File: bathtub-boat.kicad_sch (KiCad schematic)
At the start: 22 parts, among them J1 I2C, J2 SPI, J3 I2C, J4 DS18B20, SW1 MODE, SW2 RESET, SW3 POWER, SW4 A, U1 esp-01m, U2 tp4056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

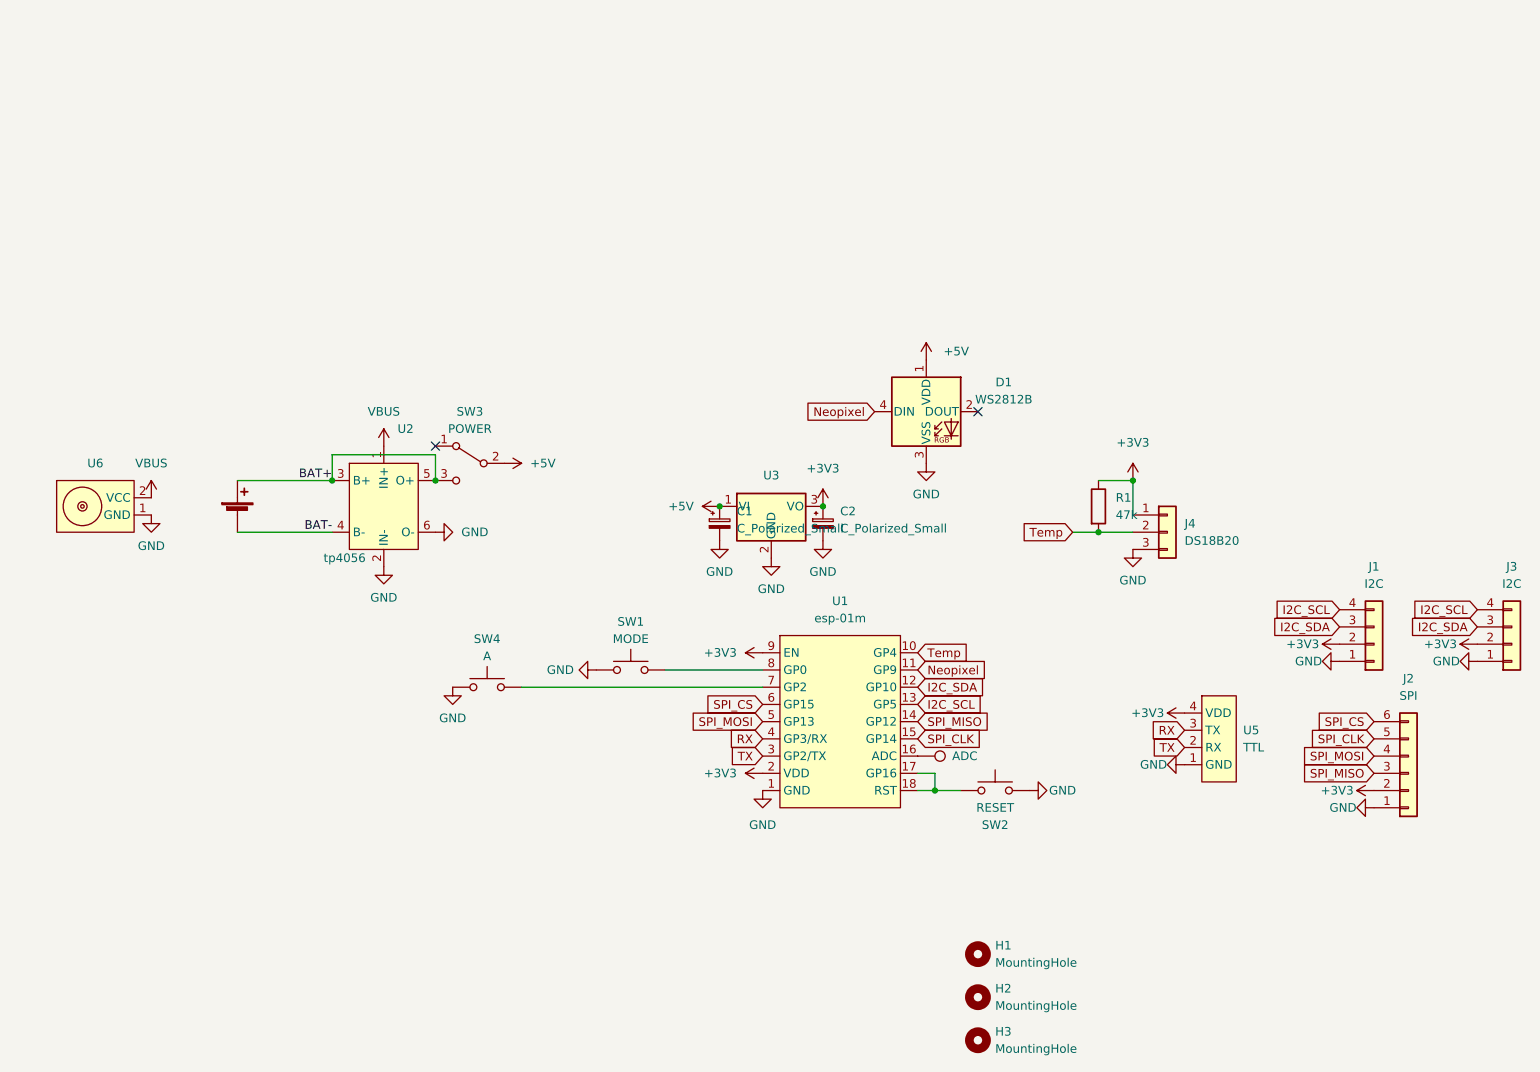
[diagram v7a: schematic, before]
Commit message: Add a top copper pour
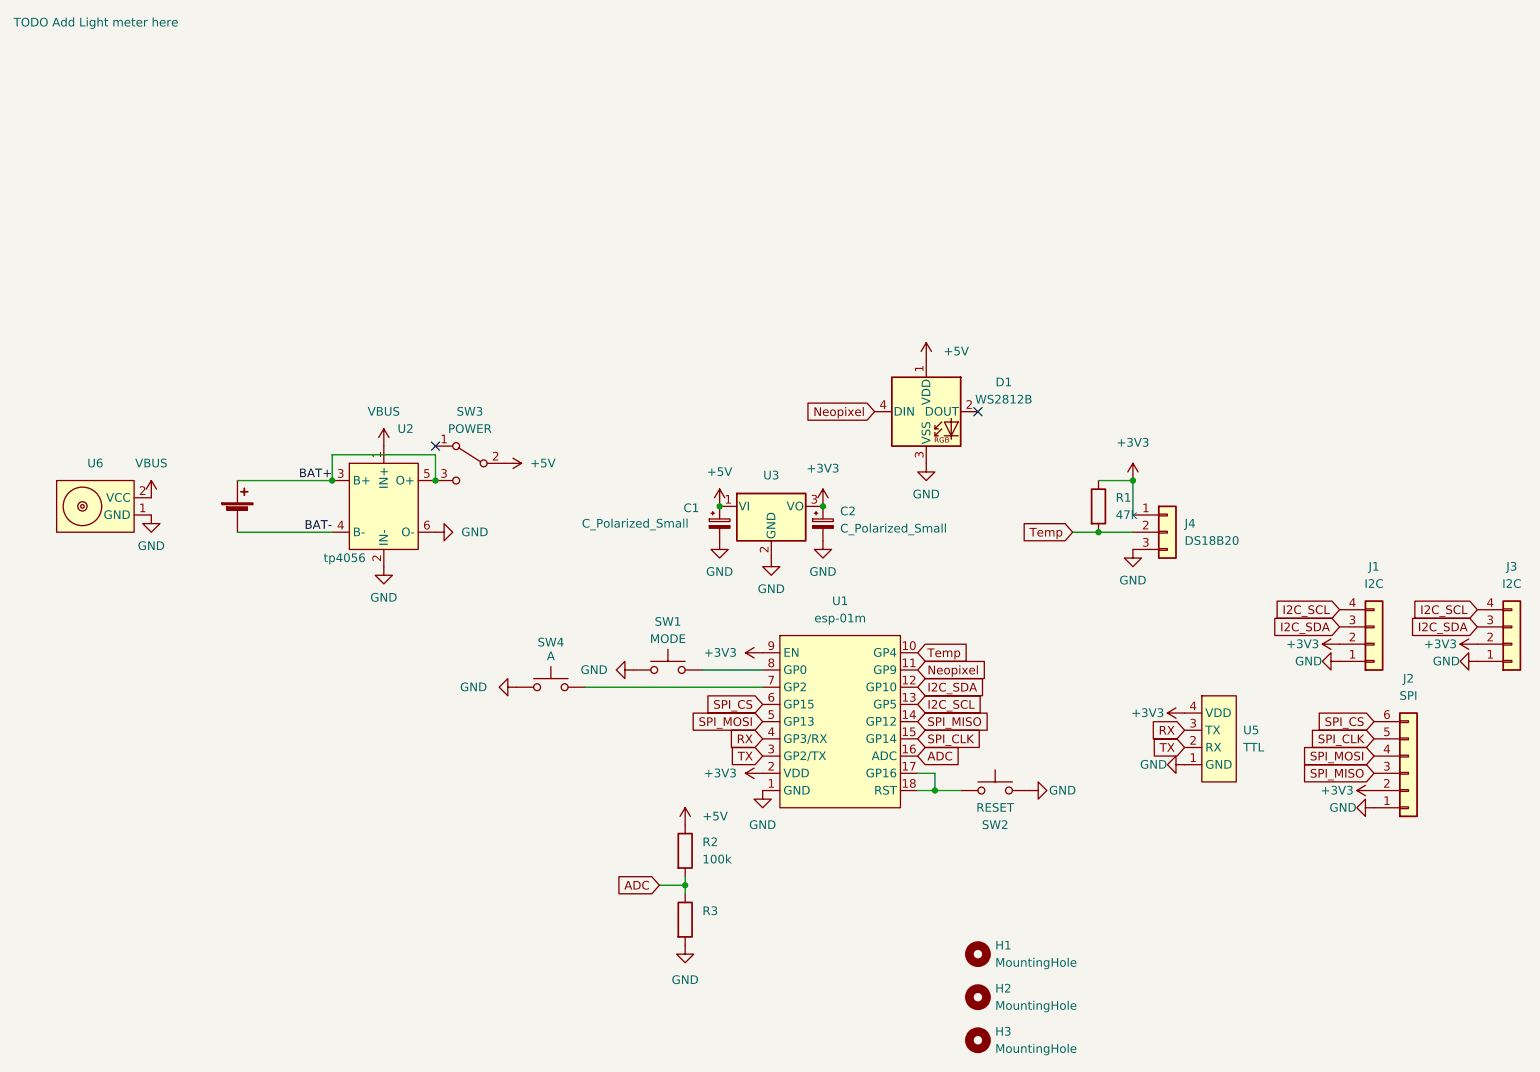
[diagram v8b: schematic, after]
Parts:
- removed TP1: ADC, TestPoint:TestPoint_THTPad_2.0x2.0mm_Drill1.0mm, symbol Connector:TestPoint
- added R2: 100k, Resistor_THT:R_Axial_DIN0204_L3.6mm_D1.6mm_P1.90mm_Vertical, symbol Device:R
- added R3: TODO Add Light meter here, Resistor_THT:R_Axial_DIN0204_L3.6mm_D1.6mm_P1.90mm_Vertical, symbol Device:R
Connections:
- net +5V: now also R2.1
- net GND: now also R3.2
- net ADC: now reaches U1.16 (ADC)
- net ADC: now also R2.2, R3.1
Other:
- moved on the sheet: SW1, SW4
